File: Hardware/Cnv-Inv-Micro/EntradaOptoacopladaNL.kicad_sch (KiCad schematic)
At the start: 3 parts, among them U22 PC817

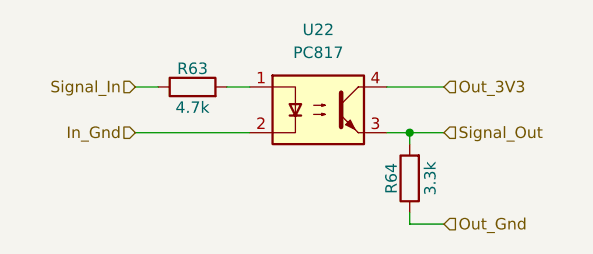
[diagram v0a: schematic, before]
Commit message: Avances en PCB conversor y inversor - Simulaciones de modulacion
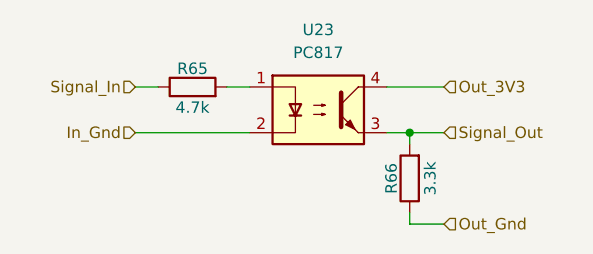
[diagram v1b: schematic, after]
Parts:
- renumbered R63 to R65, R64 to R66, U22 to U23
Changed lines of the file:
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@@
 		(dnp no)
 		(fields_autoplaced yes)
-		(property "Reference" "U22"
+		(property "Reference" "U23"
 			(at 135.89 85.09 0)
 			(effects
@@
 			(project "VFD_V1"
 				(path "/e60c11d9-ab9e-4760-a4a7-008fcec65a72/fc30a5fb-ff38-4397-8c78-21712589d910/43675de4-b717-470e-b523-b0c410cf7bca"
+					(reference "U24")
+					(unit 1)
+				)
+				(path "/e60c11d9-ab9e-4760-a4a7-008fcec65a72/fc30a5fb-ff38-4397-8c78-21712589d910/b567d3e2-0d19-45d1-8a65-79171974937b"
 					(reference "U23")
-					(unit 1)
-				)
-				(path "/e60c11d9-ab9e-4760-a4a7-008fcec65a72/fc30a5fb-ff38-4397-8c78-21712589d910/b567d3e2-0d19-45d1-8a65-79171974937b"
-					(reference "U22")
 					(unit 1)
 				)
@@
 		(on_board yes)
 		(dnp no)
-		(property "Reference" "R64"
+		(property "Reference" "R66"
 			(at 144.018 101.6 90)
 			(effects
@@
 			(project "VFD_V1"
 				(path "/e60c11d9-ab9e-4760-a4a7-008fcec65a72/fc30a5fb-ff38-4397-8c78-21712589d910/43675de4-b717-470e-b523-b0c410cf7bca"
+					(reference "R68")
+					(unit 1)
+				)
+				(path "/e60c11d9-ab9e-4760-a4a7-008fcec65a72/fc30a5fb-ff38-4397-8c78-21712589d910/b567d3e2-0d19-45d1-8a65-79171974937b"
 					(reference "R66")
-					(unit 1)
-				)
-				(path "/e60c11d9-ab9e-4760-a4a7-008fcec65a72/fc30a5fb-ff38-4397-8c78-21712589d910/b567d3e2-0d19-45d1-8a65-79171974937b"
-					(reference "R64")
 					(unit 1)
 				)
@@
 		(on_board yes)
 		(dnp no)
-		(property "Reference" "R63"
+		(property "Reference" "R65"
 			(at 121.92 89.408 90)
 			(effects
@@
 			(project "VFD_V1"
 				(path "/e60c11d9-ab9e-4760-a4a7-008fcec65a72/fc30a5fb-ff38-4397-8c78-21712589d910/43675de4-b717-470e-b523-b0c410cf7bca"
+					(reference "R67")
+					(unit 1)
+				)
+				(path "/e60c11d9-ab9e-4760-a4a7-008fcec65a72/fc30a5fb-ff38-4397-8c78-21712589d910/b567d3e2-0d19-45d1-8a65-79171974937b"
 					(reference "R65")
 					(unit 1)
 				)
-				(path "/e60c11d9-ab9e-4760-a4a7-008fcec65a72/fc30a5fb-ff38-4397-8c78-21712589d910/b567d3e2-0d19-45d1-8a65-79171974937b"
-					(reference "R63")
-					(unit 1)
-				)
